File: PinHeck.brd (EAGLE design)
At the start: 359.2 x 152.3 mm, 352 parts, among them IC1 FT232RL-REEL, IC2 PIC32MX795F512L-80I/PT, IC3 CD74HCT244E, IC4 CD74HCT244E, IC5 ULN2803A, J1 500075-1517, J11 No Load, J2 500075-1517, J3 N/A, J6 161-3507-E, P1 TC33X-2-103E, SW1 101-0134-EV, SW2 101-0134-EV, SW3 101-0134-EV, SW4 0S102011MS2QS1, U1 P8X32A-Q44, U10 74HCT2G04GV,125, U11 74HC165D,652, U12 74HC165D,652, U14 MC74HC08ADG, U15 MC74HC08ADG, U16 MC74HC08ADG, U17 MC74HC08ADG, U18 MC74HC08ADG, U19 MC74HC08ADG, U2 FT230XS-R, U20 TIP107, U21 TIP107, U22 TIP107, U23 TIP107, U24 TIP107, U25 TIP107, U26 TIP107, U27 TIP107, U28 TIP102, U29 TIP102, U3 74HC595D-Q100, U30 TIP102, U31 TIP102, U32 TIP102, U33 TIP102, U34 TIP102, U35 TIP102, U36 WS2801, U37 TIP102, U38 WS2801, U39 LM2937IMP-3.3/NOPB, U4 24LC1025-I/P, U40 TIP102, U41 TIP102, U42 TIP102, U43 TIP102, U44 TIP102, U45 TIP102, U46 TIP102, U47 TIP102, U48 TIP102, U49 TIP102, U5 74HC595D-Q100, U50 TIP102, U51 TIP102, U52 CD74HC123M96, U6 TIP102, U7 TIP102, U8 TIP102, U9 TIP102, X1 FQ7050B-8.000, X2 ECS-65-20-4X

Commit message: Added MF Logo
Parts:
- added U$2: MF_LOGOLOGO_TEXT, PP_Aesthetics:MF_LOGO_TEXT
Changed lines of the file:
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@@
 <element name="R140" library="PP_Passives" package="0805" value="4.7K" x="287.782" y="124.46"/>
 <element name="R141" library="PP_Passives" package="0805" value="4.7K" x="287.782" y="127"/>
+<element name="U$2" library="PP_Aesthetics" package="MF_LOGO_TEXT" value="MF_LOGOLOGO_TEXT" x="183.642" y="97.028"/>
 </elements>
 <signals>

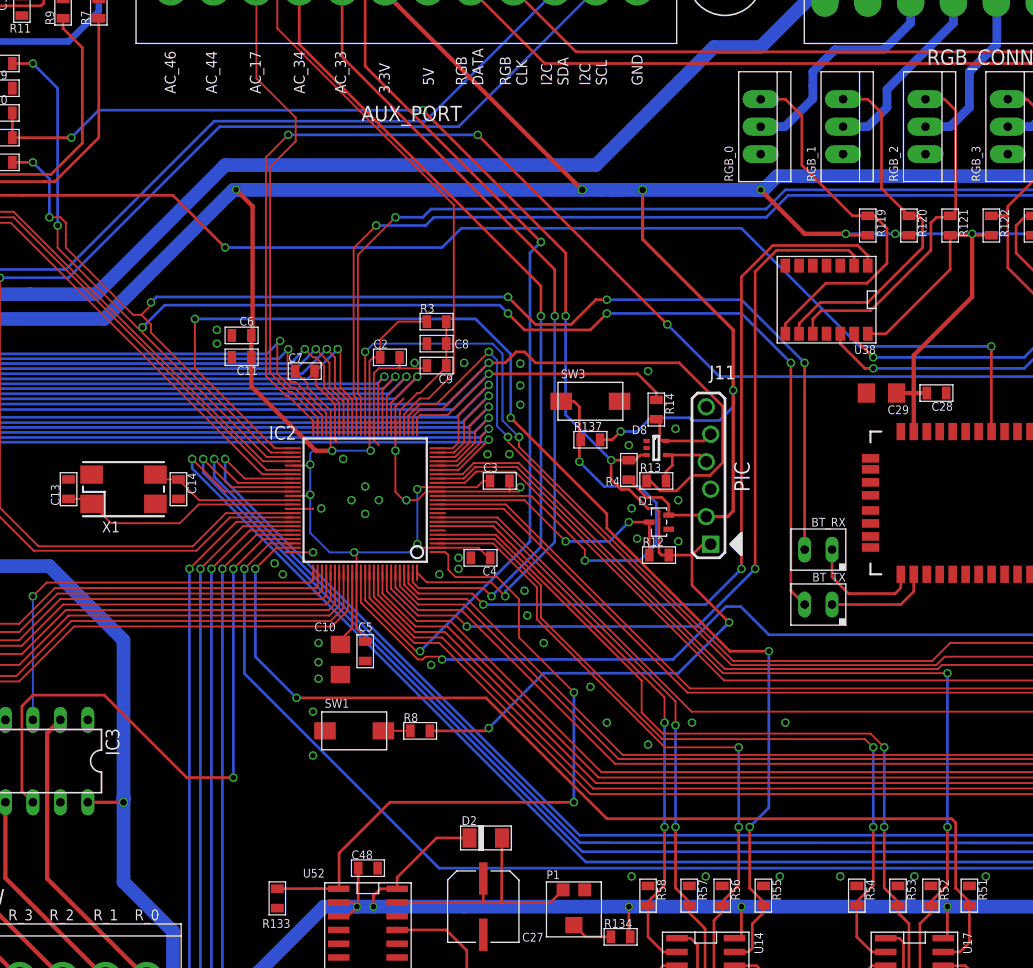
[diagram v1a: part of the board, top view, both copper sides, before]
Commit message: Swapped TX/RX on BT module.
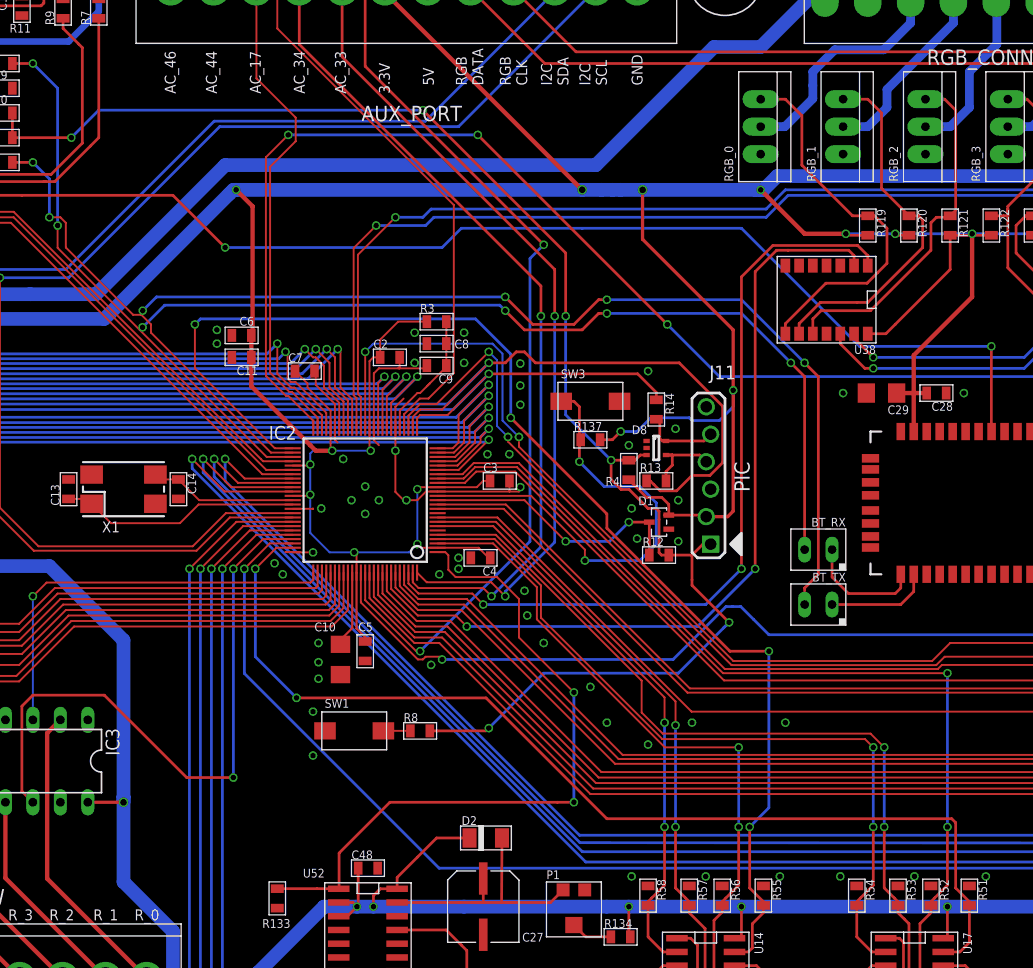
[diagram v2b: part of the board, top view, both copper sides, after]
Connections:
- net RX_PIC32: now also BT_TX.2; no longer BT_RX.2
- net TX_PIC32: now also BT_RX.2; no longer BT_TX.2
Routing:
- net RX_PIC32: track 124.8 -> 130.9 mm
- net TX_PIC32: track 137.7 -> 132.1 mm
- net PIC_SW_C_7: track 150.7 -> 150.0 mm
- net PIC_SW_C_6: track 147.2 -> 146.6 mm
- net GND: vias 107 -> 111

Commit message: Updated board layout a bit.
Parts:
- moved R11 0.25 mm to (66.3, 166.1)
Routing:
- net FT_3.3V: track 45.3 -> 44.8 mm
